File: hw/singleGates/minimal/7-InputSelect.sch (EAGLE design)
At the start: 32 parts, among them Q1 BC817, Q10 BC817, Q11 BC817, Q12 BC817, Q13 BC817, Q14 BC817, Q17 BC817, Q2 BC817, Q3 BC817, Q4 BC817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

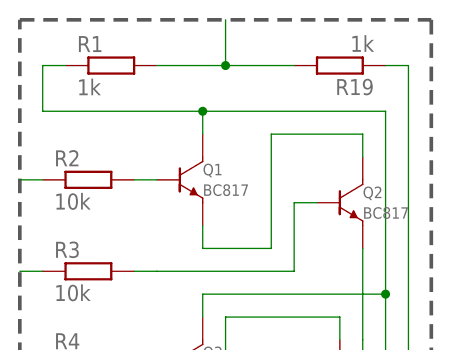
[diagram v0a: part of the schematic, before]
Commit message: Add led output and prepare first alu slice
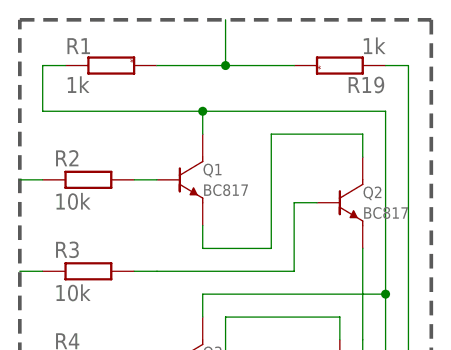
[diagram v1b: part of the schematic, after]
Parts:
- R1, R19: device p.peter-gator:R-EU_R0603 -> p.peter-rcl:R-EU-MARKEDR0603
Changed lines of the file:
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@@
 <part name="R2" library="p.peter-gator" deviceset="R-EU_" device="R0603" value="10k"/>
 <part name="R3" library="p.peter-gator" deviceset="R-EU_" device="R0603" value="10k"/>
-<part name="R1" library="p.peter-gator" deviceset="R-EU_" device="R0603" value="1k"/>
+<part name="R1" library="p.peter-rcl" deviceset="R-EU-MARKED" device="R0603" value="1k"/>
 <part name="R4" library="p.peter-gator" deviceset="R-EU_" device="R0603" value="10k"/>
 <part name="R5" library="p.peter-gator" deviceset="R-EU_" device="R0603" value="10k"/>
@@
 <part name="R15" library="p.peter-gator" deviceset="R-EU_" device="R0603" value="10k"/>
 <part name="R18" library="p.peter-gator" deviceset="R-EU_" device="R0603" value="10k"/>
-<part name="R19" library="p.peter-gator" deviceset="R-EU_" device="R0603" value="1k"/>
+<part name="R19" library="p.peter-rcl" deviceset="R-EU-MARKED" device="R0603" value="1k"/>
 <part name="Q1" library="p.peter-gator" deviceset="TRANSISTOR-NPN-GENERIC" device="-SOT23-BEC" technology="DEFAULT" value="BC817"/>
 <part name="Q2" library="p.peter-gator" deviceset="TRANSISTOR-NPN-GENERIC" device="-SOT23-BEC" technology="DEFAULT" value="BC817"/>
